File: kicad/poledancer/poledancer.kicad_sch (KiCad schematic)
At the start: 35 parts, among them J1 Conn_02x20_Odd_Even, J2 Conn_01x02, J3 Conn_01x01, Q1 MMBT3904, U1 PS508, U2 PS508, U3 TL074, U4 PCA9555D, U5 M24C02-WMN, U8 LM4040AIM3-2.5

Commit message: continue placement
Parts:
- added C17: 2u2, Capacitor_SMD:C_0603_1608Metric, symbol Device:C
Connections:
- net GND: now also C17.2
- net LED_CTRL: now also U4.20 (IO1_7); no longer U4.11 (IO0_7)
- net VCF_SIG1_EN: now also U4.10 (IO0_6); no longer U4.13 (IO1_0)
- net VCF_SIG2_CTRL0: now also U4.7 (IO0_3); no longer U4.8 (IO0_4)
- net VCF_SIG2_CTRL1: now also U4.8 (IO0_4); no longer U4.9 (IO0_5)
- net VCF_SIG2_CTRL2: now also U4.9 (IO0_5); no longer U4.10 (IO0_6)
- net VCF_SIG2_EN: now also U4.11 (IO0_7); no longer U4.14 (IO1_1)
- net VREF_2.5V: now also C17.1
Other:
- moved on the sheet: D1, R3

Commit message: placement looks ok.  Some tweakin, yes, but call it workable.
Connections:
- net INPUT1: now also U3.8, U3.9 (-); no longer U3.13 (-), U3.14
- net INPUT2: now also U3.13 (-), U3.14; no longer U3.8, U3.9 (-)
- net at R1.2, U3.10 (+): now also U1.8 (D); no longer U2.8 (D)
- net at R2.2, U3.12 (+): now also U2.8 (D); no longer U1.8 (D)
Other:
- moved on the sheet: R1, R2, U3C, U3D
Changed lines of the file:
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@@
     )
   )
-  (symbol (lib_id "Amplifier_Operational:TL074") (at 88.9 204.47 0) (mirror x) (unit 3)
+  (symbol (lib_id "Amplifier_Operational:TL074") (at 88.9 135.89 0) (mirror x) (unit 3)
     (in_bom yes) (on_board yes) (dnp no) (fields_autoplaced)
-    (property "Reference" "U3" (at 88.9 195.6902 0)
-      (effects (font (size 1.27 1.27)))
-    )
-    (property "Value" "TL074" (at 88.9 198.2271 0)
-      (effects (font (size 1.27 1.27)))
-    )
-    (property "Footprint" "Package_SO:TSSOP-14_4.4x5mm_P0.65mm" (at 87.63 207.01 0)
-      (effects (font (size 1.27 1.27)) hide)
-    )
-    (property "Datasheet" "http://www.ti.com/lit/ds/symlink/tl071.pdf" (at 90.17 209.55 0)
-      (effects (font (size 1.27 1.27)) hide)
-    )
-    (property "LCSC" "C96507" (at 88.9 114.3 0)
+    (property "Reference" "U3" (at 88.9 127.1102 0)
+      (effects (font (size 1.27 1.27)))
+    )
+    (property "Value" "TL074" (at 88.9 129.6471 0)
+      (effects (font (size 1.27 1.27)))
+    )
+    (property "Footprint" "Package_SO:TSSOP-14_4.4x5mm_P0.65mm" (at 87.63 138.43 0)
+      (effects (font (size 1.27 1.27)) hide)
+    )
+    (property "Datasheet" "http://www.ti.com/lit/ds/symlink/tl071.pdf" (at 90.17 140.97 0)
+      (effects (font (size 1.27 1.27)) hide)
+    )
+    (property "LCSC" "C96507" (at 88.9 45.72 0)
       (effects (font (size 1.27 1.27)) hide)
     )
@@
     )
   )
-  (symbol (lib_id "Device:R") (at 73.66 143.51 180) (unit 1)
-    (in_bom yes) (on_board yes) (dnp no)
-    (property "Reference" "R2" (at 69.215 142.24 0)
-      (effects (font (size 1.27 1.27)) (justify right))
-    )
-    (property "Value" "100k" (at 67.31 144.78 0)
-      (effects (font (size 1.27 1.27)) (justify right))
-    )
-    (property "Footprint" "Resistor_SMD:R_0603_1608Metric" (at 75.438 143.51 90)
-      (effects (font (size 1.27 1.27)) hide)
-    )
-    (property "Datasheet" "~" (at 73.66 143.51 0)
-      (effects (font (size 1.27 1.27)) hide)
-    )
-    (property "LCSC" "C25803" (at 73.66 143.51 0)
+  (symbol (lib_id "Device:R") (at 72.39 212.09 180) (unit 1)
+    (in_bom yes) (on_board yes) (dnp no)
+    (property "Reference" "R2" (at 67.945 210.82 0)
+      (effects (font (size 1.27 1.27)) (justify right))
+    )
+    (property "Value" "100k" (at 66.04 213.36 0)
+      (effects (font (size 1.27 1.27)) (justify right))
+    )
+    (property "Footprint" "Resistor_SMD:R_0603_1608Metric" (at 74.168 212.09 90)
+      (effects (font (size 1.27 1.27)) hide)
+    )
+    (property "Datasheet" "~" (at 72.39 212.09 0)
+      (effects (font (size 1.27 1.27)) hide)
+    )
+    (property "LCSC" "C25803" (at 72.39 212.09 0)
       (effects (font (size 1.27 1.27)) hide)
     )
@@
     )
   )
-  (symbol (lib_id "Amplifier_Operational:TL074") (at 88.9 135.89 0) (mirror x) (unit 4)
+  (symbol (lib_id "Amplifier_Operational:TL074") (at 88.9 204.47 0) (mirror x) (unit 4)
     (in_bom yes) (on_board yes) (dnp no) (fields_autoplaced)
-    (property "Reference" "U3" (at 88.9 127.1102 0)
-      (effects (font (size 1.27 1.27)))
-    )
-    (property "Value" "TL074" (at 88.9 129.6471 0)
-      (effects (font (size 1.27 1.27)))
-    )
-    (property "Footprint" "Package_SO:TSSOP-14_4.4x5mm_P0.65mm" (at 87.63 138.43 0)
-      (effects (font (size 1.27 1.27)) hide)
-    )
-    (property "Datasheet" "http://www.ti.com/lit/ds/symlink/tl071.pdf" (at 90.17 140.97 0)
-      (effects (font (size 1.27 1.27)) hide)
-    )
-    (property "LCSC" "C96507" (at 88.9 45.72 0)
+    (property "Reference" "U3" (at 88.9 195.6902 0)
+      (effects (font (size 1.27 1.27)))
+    )
+    (property "Value" "TL074" (at 88.9 198.2271 0)
+      (effects (font (size 1.27 1.27)))
+    )
+    (property "Footprint" "Package_SO:TSSOP-14_4.4x5mm_P0.65mm" (at 87.63 207.01 0)
+      (effects (font (size 1.27 1.27)) hide)
+    )
+    (property "Datasheet" "http://www.ti.com/lit/ds/symlink/tl071.pdf" (at 90.17 209.55 0)
+      (effects (font (size 1.27 1.27)) hide)
+    )
+    (property "LCSC" "C96507" (at 88.9 114.3 0)
       (effects (font (size 1.27 1.27)) hide)
     )
@@
     )
   )
-  (symbol (lib_id "Device:R") (at 72.39 212.09 180) (unit 1)
+  (symbol (lib_id "Device:R") (at 73.66 143.51 180) (unit 1)
     (in_bom yes) (on_board yes) (dnp no) (fields_autoplaced)
-    (property "Reference" "R1" (at 74.168 211.2553 0)
-      (effects (font (size 1.27 1.27)) (justify right))
-    )
-    (property "Value" "100k" (at 74.168 213.7922 0)
-      (effects (font (size 1.27 1.27)) (justify right))
-    )
-    (property "Footprint" "Resistor_SMD:R_0603_1608Metric" (at 74.168 212.09 90)
-      (effects (font (size 1.27 1.27)) hide)
-    )
-    (property "Datasheet" "~" (at 72.39 212.09 0)
-      (effects (font (size 1.27 1.27)) hide)
-    )
-    (property "LCSC" "C25803" (at 72.39 212.09 0)
-      (effects (font (size 1.27 1.27)) hide)
-    )
+    (property "Reference" "R1" (at 75.438 142.6753 0)
+      (effects (font (size 1.27 1.27)) (justify right))
+    )
+    (property "Value" "100k" (at 75.438 145.2122 0)
+      (effects (font (size 1.27 1.27)) (justify right))
+    )
+    (property "Footprint" "Resistor_SMD:R_0603_1608Metric" (at 75.438 143.51 90)
+      (effects (font (size 1.27 1.27)) hide)
+    )
+    (property "Datasheet" "~" (at 73.66 143.51 0)
+      (effects (font (size 1.27 1.27)) hide)
+    )
+    (property "LCSC" "C25803" (at 73.66 143.51 0)
+      (effects (font (size 1.27 1.27)) hide)
+    )

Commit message: a bit more tweaking on placement
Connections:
- net VCF_SIG1_CTRL0: now also U4.5 (IO0_1); no longer U4.4 (IO0_0)
- net VCF_SIG1_CTRL1: now also U4.6 (IO0_2); no longer U4.5 (IO0_1)
- net VCF_SIG1_CTRL2: now also U4.7 (IO0_3); no longer U4.6 (IO0_2)
- net VCF_SIG1_EN: now also U4.4 (IO0_0); no longer U4.10 (IO0_6)
- net VCF_SIG2_CTRL0: now also U4.9 (IO0_5); no longer U4.7 (IO0_3)
- net VCF_SIG2_CTRL1: now also U4.10 (IO0_6); no longer U4.8 (IO0_4)
- net VCF_SIG2_CTRL2: now also U4.11 (IO0_7); no longer U4.9 (IO0_5)
- net VCF_SIG2_EN: now also U4.8 (IO0_4); no longer U4.11 (IO0_7)
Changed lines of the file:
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@@
     (effects (font (size 1.27 1.27)) (justify left bottom))
   )
-  (label "VCF_SIG2_CTRL1" (at 215.9 57.15 180) (fields_autoplaced)
+  (label "VCF_SIG2_CTRL1" (at 215.9 62.23 180) (fields_autoplaced)
     (effects (font (size 1.27 1.27)) (justify right bottom))
   )
@@
     (effects (font (size 1.27 1.27)) (justify right bottom))
   )
-  (label "VCF_SIG2_CTRL0" (at 215.9 54.61 180) (fields_autoplaced)
-    (effects (font (size 1.27 1.27)) (justify right bottom))
-  )
-  (label "VCF_SIG2_EN" (at 215.9 64.77 180) (fields_autoplaced)
+  (label "VCF_SIG2_CTRL0" (at 215.9 59.69 180) (fields_autoplaced)
+    (effects (font (size 1.27 1.27)) (justify right bottom))
+  )
+  (label "VCF_SIG2_EN" (at 215.9 57.15 180) (fields_autoplaced)
     (effects (font (size 1.27 1.27)) (justify right bottom))
   )
@@
     (effects (font (size 1.27 1.27)) (justify left bottom))
   )
-  (label "VCF_SIG1_CTRL0" (at 215.9 46.99 180) (fields_autoplaced)
+  (label "VCF_SIG1_CTRL0" (at 215.9 49.53 180) (fields_autoplaced)
     (effects (font (size 1.27 1.27)) (justify right bottom))
   )
@@
     (effects (font (size 1.27 1.27)) (justify right bottom))
   )
-  (label "VCF_SIG1_EN" (at 215.9 62.23 180) (fields_autoplaced)
+  (label "VCF_SIG1_EN" (at 215.265 46.99 180) (fields_autoplaced)
     (effects (font (size 1.27 1.27)) (justify right bottom))
   )
@@
     (effects (font (size 1.27 1.27)) (justify left bottom))
   )
-  (label "VCF_SIG1_CTRL1" (at 215.9 49.53 180) (fields_autoplaced)
+  (label "VCF_SIG1_CTRL1" (at 215.9 52.07 180) (fields_autoplaced)
     (effects (font (size 1.27 1.27)) (justify right bottom))
   )
@@
     (effects (font (size 1.27 1.27)) (justify left bottom))
   )
-  (label "VCF_SIG2_CTRL2" (at 215.9 59.69 180) (fields_autoplaced)
+  (label "VCF_SIG2_CTRL2" (at 215.9 64.77 180) (fields_autoplaced)
     (effects (font (size 1.27 1.27)) (justify right bottom))
   )
@@
     (effects (font (size 1.27 1.27)) (justify right bottom))
   )
-  (label "VCF_SIG1_CTRL2" (at 215.9 52.07 180) (fields_autoplaced)
-    (effects (font (size 1.27 1.27)) (justify right bottom))
-  )
+  (label "VCF_SIG1_CTRL2" (at 215.9 54.61 180) (fields_autoplaced)
+    (effects (font (size 1.27 1.27)) (justify right bottom))
+  )

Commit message: routing.  it might go pretty quick!
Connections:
- net LED_CTRL: now also U4.13 (IO1_0); no longer U4.20 (IO1_7)
- net QVCA_INVERT: now also U4.14 (IO1_1); no longer U4.18 (IO1_5)
- net REZ_STAGE2_EN: now also U4.19 (IO1_6); no longer U4.16 (IO1_3)
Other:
- moved on the sheet: D1, R3

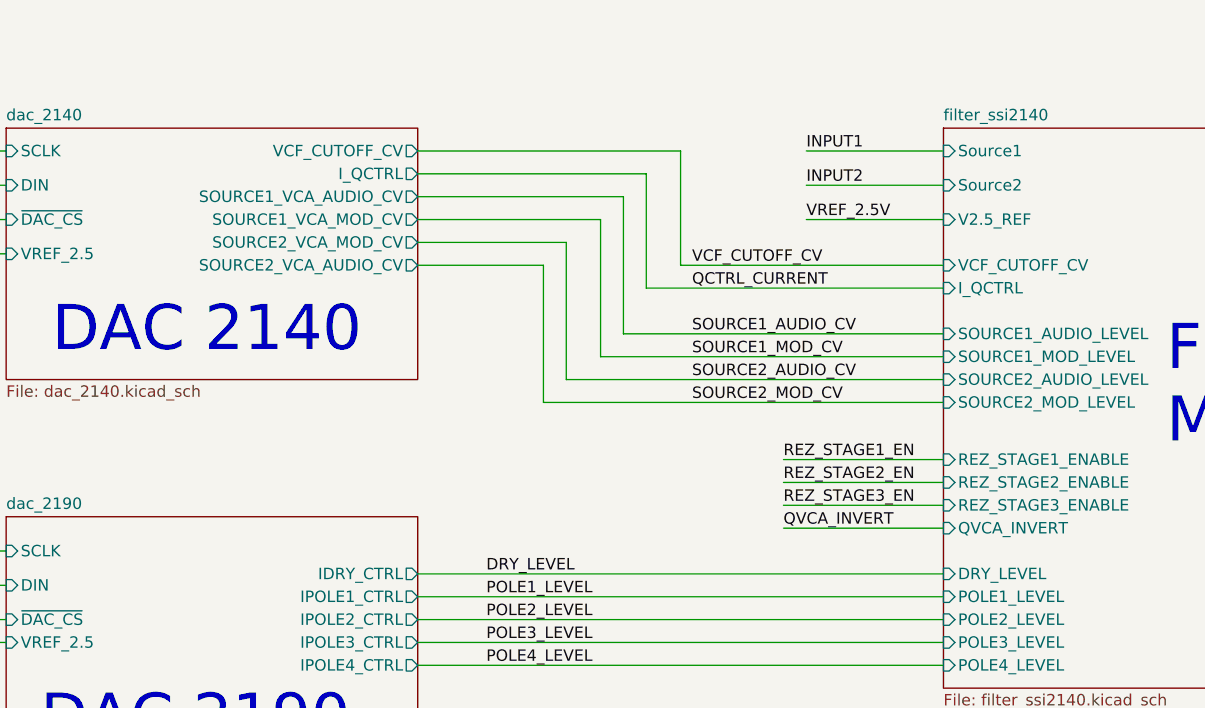
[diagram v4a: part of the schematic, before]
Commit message: start routing power
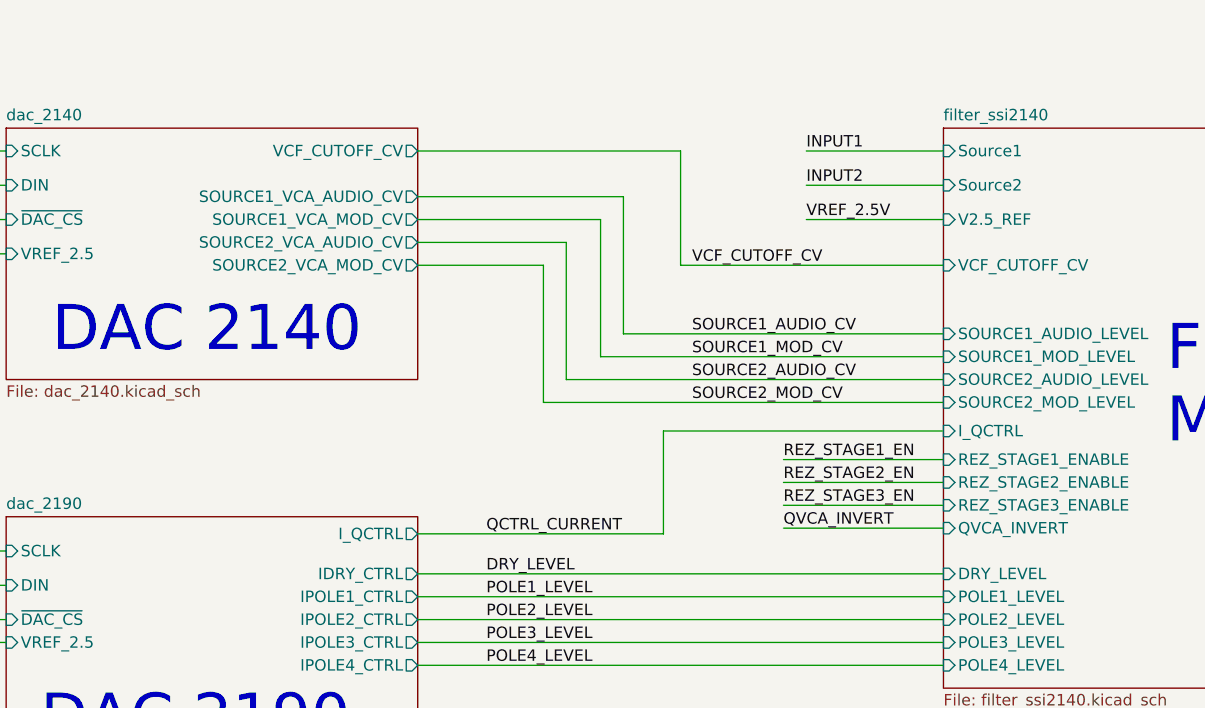
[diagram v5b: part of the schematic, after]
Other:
- sheet dac_2140 ports: added none; removed I_QCTRL
- sheet dac_2190 ports: added I_QCTRL; removed none
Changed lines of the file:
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@@
     (stroke (width 0) (type default))
   )
-  (wire (pts (xy 236.22 152.4) (xy 269.24 152.4))
-    (stroke (width 0) (type default))
-  )
   (wire (pts (xy 82.55 54.61) (xy 109.22 54.61))
     (stroke (width 0) (type default))
@@
     (stroke (width 0) (type default))
   )
+  (wire (pts (xy 210.82 179.705) (xy 238.125 179.705))
+    (stroke (width 0) (type default))
+  )
   (wire (pts (xy 251.46 176.53) (xy 269.24 176.53))
     (stroke (width 0) (type default))
@@
     (stroke (width 0) (type default))
   )
-  (wire (pts (xy 236.22 139.7) (xy 236.22 152.4))
-    (stroke (width 0) (type default))
-  )
   (wire (pts (xy 276.86 256.54) (xy 281.94 256.54))
     (stroke (width 0) (type default))
@@
     (stroke (width 0) (type default))
   )
+  (wire (pts (xy 238.125 168.275) (xy 238.125 179.705))
+    (stroke (width 0) (type default))
+  )
   (polyline (pts (xy 295.91 20.32) (xy 306.07 20.32))
     (stroke (width 0) (type dash))
@@
     (stroke (width 0) (type dash))
   )
-  (wire (pts (xy 210.82 139.7) (xy 236.22 139.7))
-    (stroke (width 0) (type default))
-  )
   (wire (pts (xy 109.22 34.29) (xy 109.22 39.37))
     (stroke (width 0) (type default))
@@
     (stroke (width 0) (type default))
   )
+  (wire (pts (xy 269.24 168.275) (xy 238.125 168.275))
+    (stroke (width 0) (type default))
+  )
   (wire (pts (xy 82.55 72.39) (xy 97.79 72.39))
     (stroke (width 0) (type default))
@@
     (effects (font (size 1.27 1.27)) (justify left bottom))
   )
-  (label "QCTRL_CURRENT" (at 241.3 152.4 0) (fields_autoplaced)
+  (label "QCTRL_CURRENT" (at 218.44 179.705 0) (fields_autoplaced)
     (effects (font (size 1.27 1.27)) (justify left bottom))
   )
@@
       (effects (font (size 1.27 1.27)) (justify left))
     )
+    (pin "I_QCTRL" output (at 210.82 179.705 0)
+      (effects (font (size 1.27 1.27)) (justify right))
+    )
     (instances
       (project "poledancer"
@@
       (effects (font (size 1.27 1.27)) (justify left))
     )
-    (pin "I_QCTRL" input (at 269.24 152.4 180)
+    (pin "I_QCTRL" input (at 269.24 168.275 180)
       (effects (font (size 1.27 1.27)) (justify left))
     )
@@
       (effects (font (size 1.27 1.27)) (justify right))
     )
-    (pin "SOURCE2_VCA_MOD_CV" output (at 210.82 147.32 0)
+    (pin "SOURCE2_VCA_MOD_CV" output (at 210.82 149.86 0)
       (effects (font (size 1.27 1.27)) (justify right))
     )
-    (pin "SOURCE2_VCA_AUDIO_CV" output (at 210.82 149.86 0)
+    (pin "SOURCE2_VCA_AUDIO_CV" output (at 210.82 147.32 0)
       (effects (font (size 1.27 1.27)) (justify right))
     )
@@
       (effects (font (size 1.27 1.27)) (justify left))
     )
-    (pin "I_QCTRL" output (at 210.82 139.7 0)
-      (effects (font (size 1.27 1.27)) (justify right))
-    )
     (instances

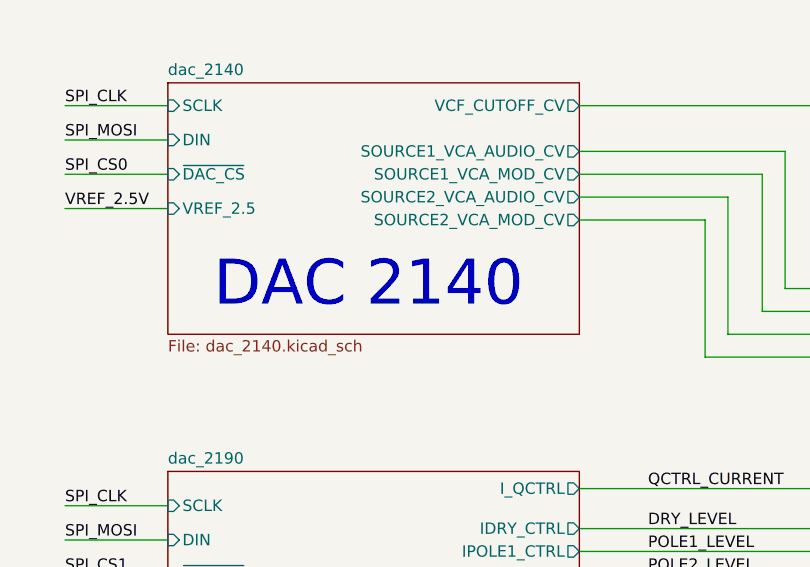
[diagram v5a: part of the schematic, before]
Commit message: renaming some DAC stuff
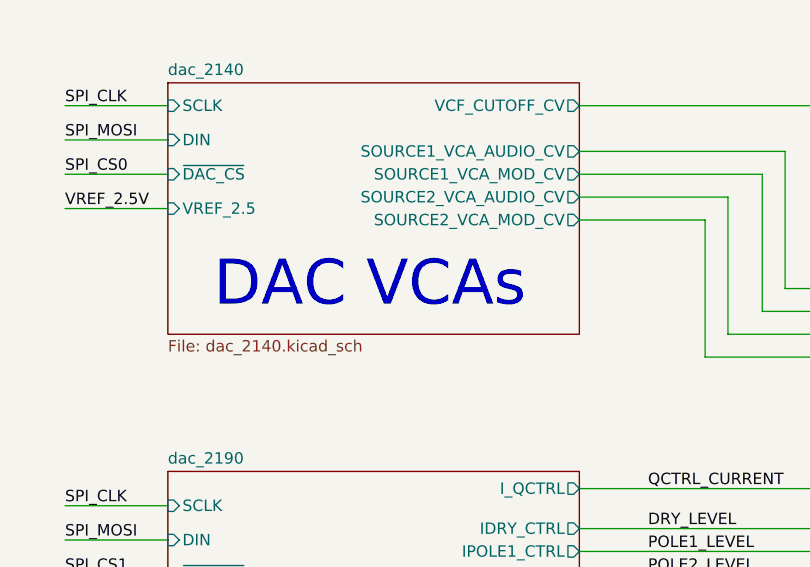
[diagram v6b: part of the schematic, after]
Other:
- note added: "DAC VCAs"
- note removed: "DAC 2140"
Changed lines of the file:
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@@
     (effects (font (size 1.27 1.27)) (justify left bottom))
   )
-  (text "DAC 2140" (at 170.18 160.02 0)
+  (text "DAC VCAs" (at 170.18 160.02 0)
     (effects (font (size 5.0038 5.0038)) (justify left bottom))
   )

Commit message: poledancer: zero unrouted!  now to de-uglify the routing
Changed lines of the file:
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@@
   (junction (at 109.22 74.93) (diameter 0) (color 0 0 0 0)
-  )
-  (junction (at 109.22 34.29) (diameter 0) (color 0 0 0 0)
   )
   (junction (at 270.51 247.65) (diameter 0) (color 0 0 0 0)
@@
     (stroke (width 0) (type default))
   )
-  (wire (pts (xy 109.22 31.75) (xy 109.22 34.29))
-    (stroke (width 0) (type default))
-  )

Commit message: geo reannotate
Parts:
- renumbered C17 to C21, C3 to C28, C6 to C29, C5 to C31, C4 to C33, C1 to C35, C2 to C37, C7 to C42, C8 to C43, D2 to D1, D1 to D2, H4 to H1, H1 to H4, J3 to J1, J1 to J3, R30 to R52, R82 to R58, R83 to R62, R2 to R63, R1 to R64, R16 to R65, R4 to R75, R3 to R82, R84 to R83, TP11 to TP8, U3 to U10, U2 to U11, U5 to U12, U4 to U13, U1 to U9
